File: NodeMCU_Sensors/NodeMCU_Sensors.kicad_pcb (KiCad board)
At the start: 2 copper layers, 71.1 x 40.6 mm, 12 parts, among them J1 Conn_02x15_Odd_Even, J2 Conn_02x15_Odd_Even, SW1 SW_Push

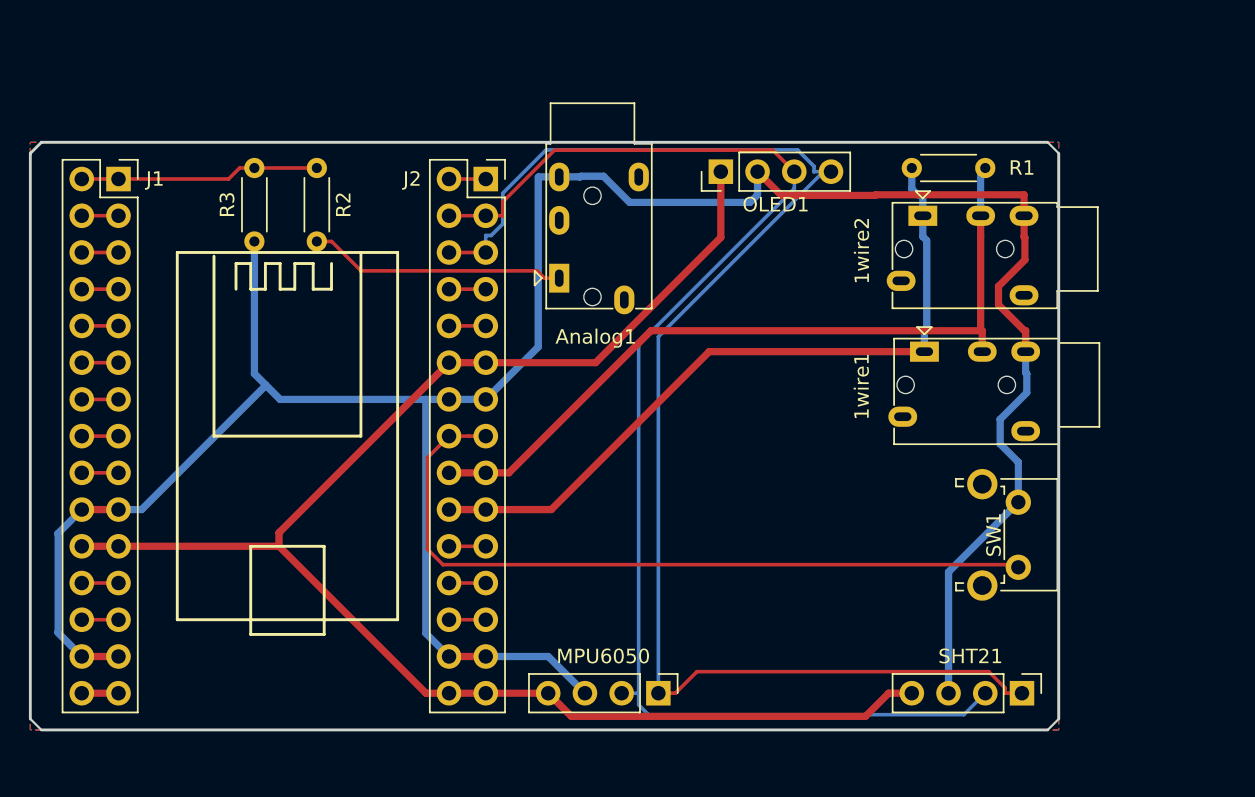
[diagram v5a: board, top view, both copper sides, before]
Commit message: Add 3V3 supply to analog pin and re-route
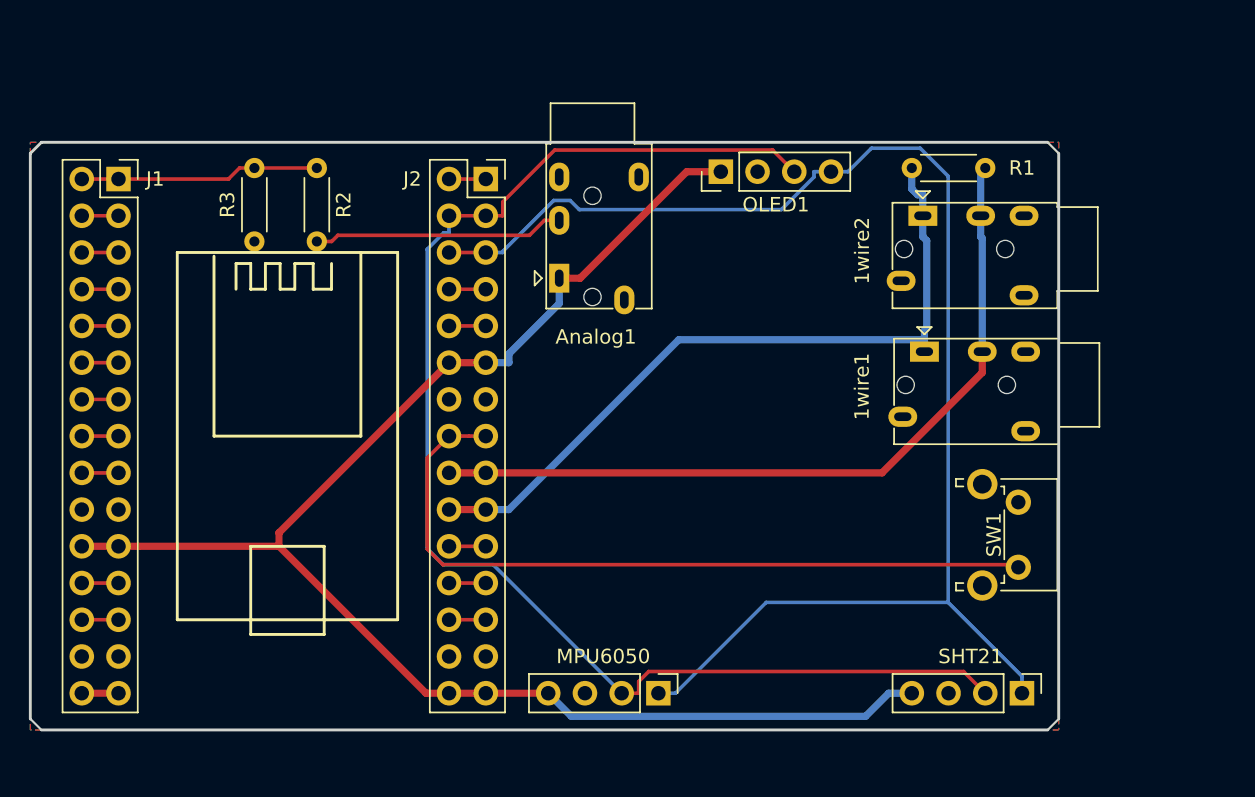
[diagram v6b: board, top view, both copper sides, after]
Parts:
- R2: value 39K -> 23.2K
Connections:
- Analog1 pad 1: Net-(Analog1-Pad1) -> 3V3
- R2 pad 2: Net-(Analog1-Pad1) -> Net-(Analog1-Pad2)
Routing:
- net GND: track 178.3 -> 0.00 mm
- net Net-(Analog1-Pad1): track 17.8 -> 0.00 mm
- net Net-(Analog1-Pad2): track 0.00 -> 17.4 mm
- net 3V3: track 107.4 -> 106.2 mm
- net D1: track 94.3 -> 95.3 mm
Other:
- board text added: "NodeMCU Sensor Node http://makesmart.io/ PCB: Whatnick INC v0.1 30/01/2018"
- board text removed: "NodeMCU Sensor Node Whatnick INC v0.1 28/01/2018"

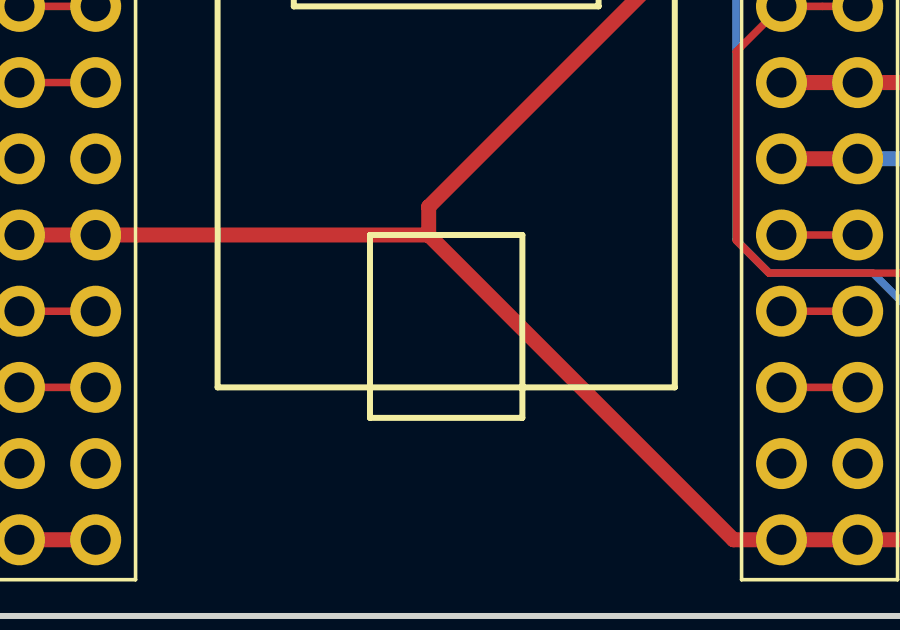
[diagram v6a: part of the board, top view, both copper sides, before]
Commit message: Adde makesmart logo
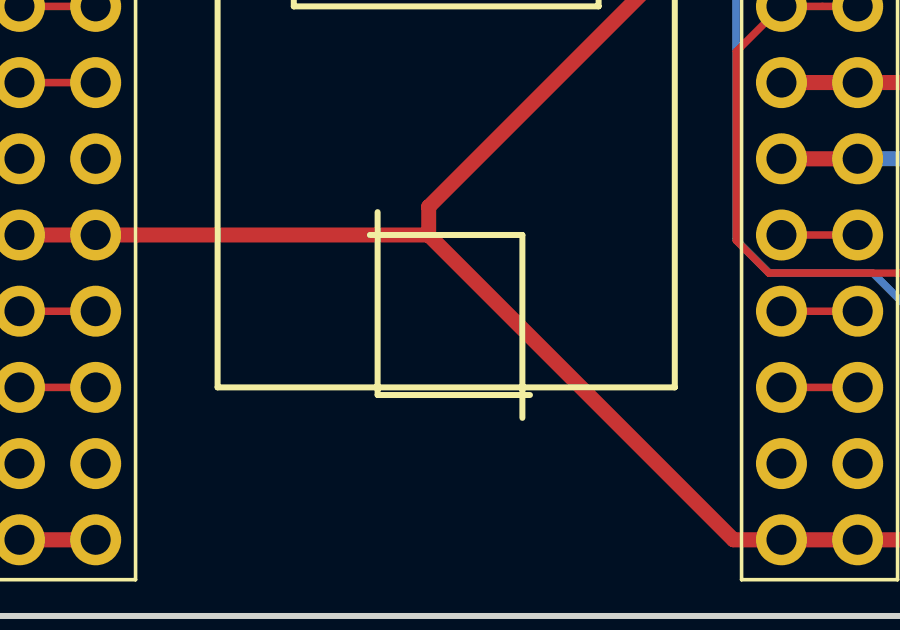
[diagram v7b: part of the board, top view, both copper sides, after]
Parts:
- added G1: LOGO, project_footprints:makeSmart_logo, B.Cu at (111.5, 81.0)
- added G2: Logo_Open_Hardware_Small, Symbols:OSHW-Logo2_7.3x6mm_SilkScreen, B.Cu at (111.3, 92.5)
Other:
- board text added: "TAPR"

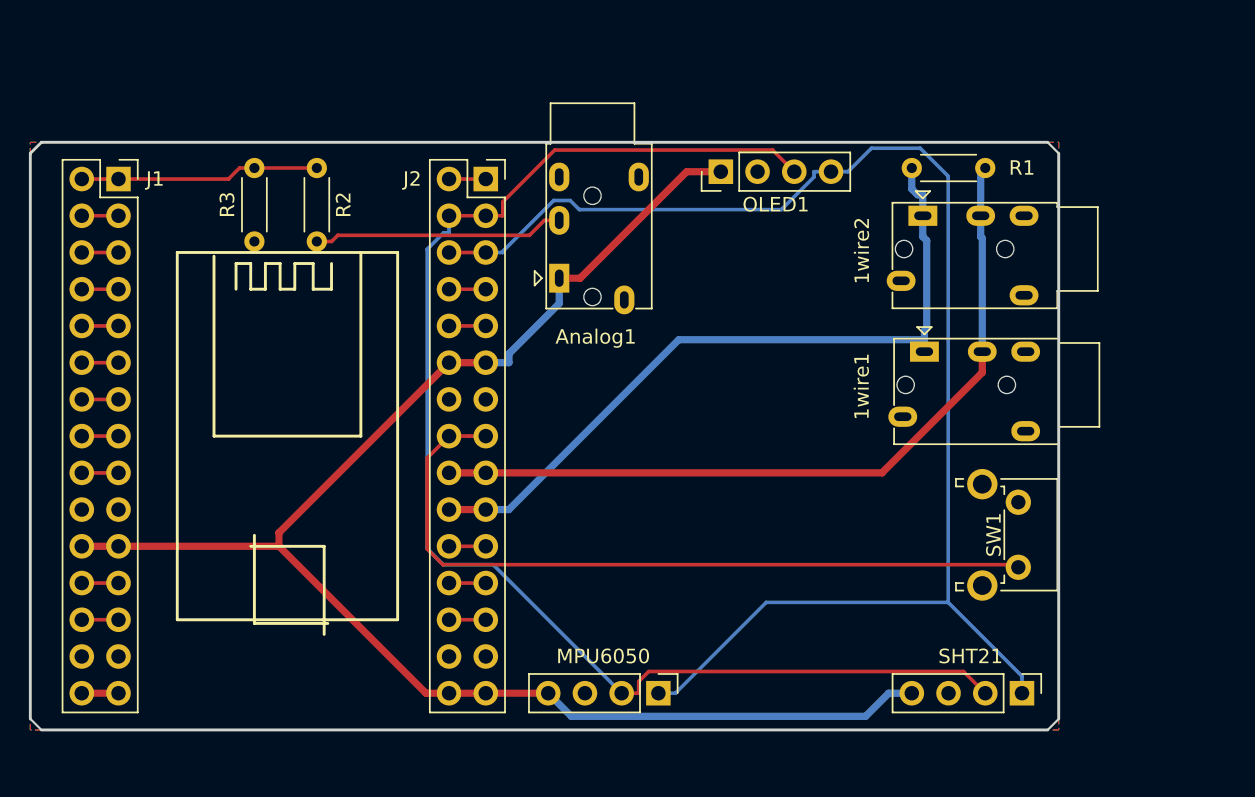
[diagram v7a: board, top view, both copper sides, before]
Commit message: Address #1 for V2 board
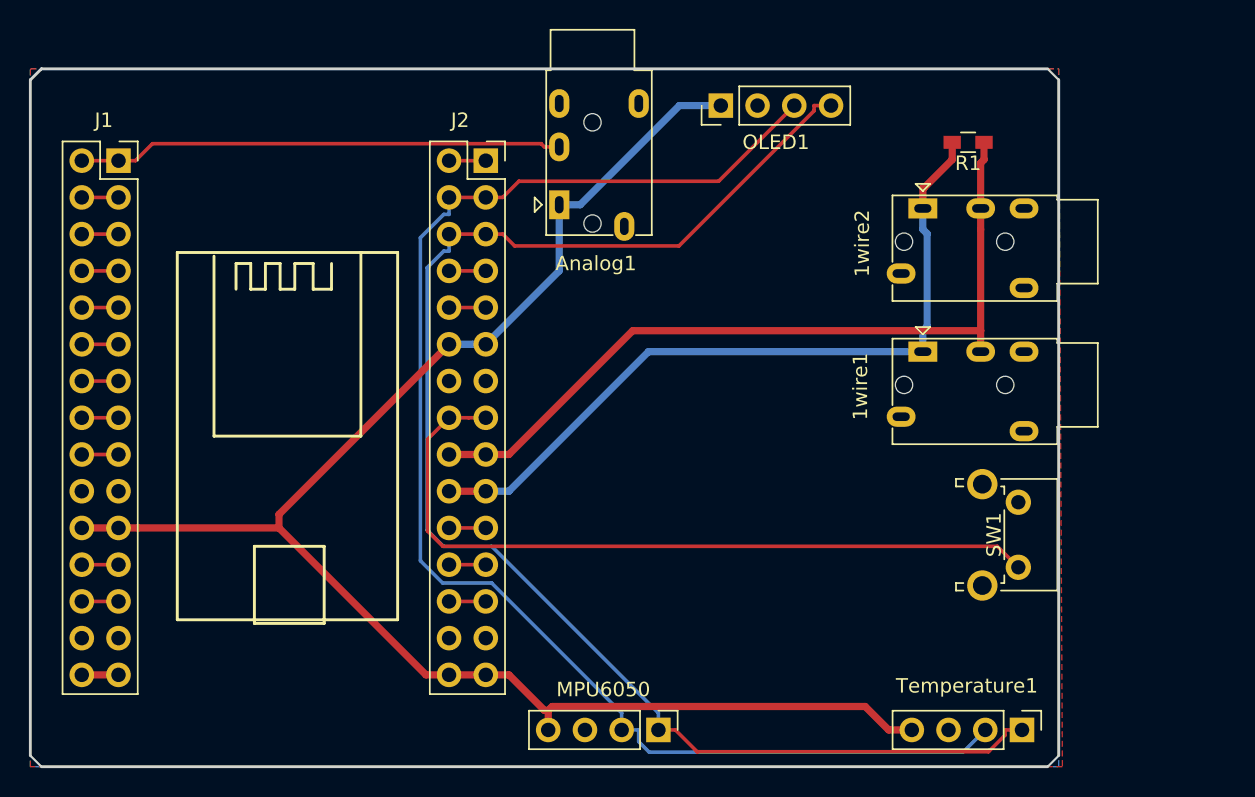
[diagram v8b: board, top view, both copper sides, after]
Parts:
- removed R2: 23.2K, Resistors_THT:R_Axial_DIN0204_L3.6mm_D1.6mm_P5.08mm_Horizontal
- removed R3: 10K, Resistors_THT:R_Axial_DIN0204_L3.6mm_D1.6mm_P5.08mm_Horizontal
- removed SHT21: Conn_01x04, Socket_Strips:Socket_Strip_Straight_1x04_Pitch2.54mm
- added Temperature1: Conn_01x04, Socket_Strips:Socket_Strip_Straight_1x04_Pitch2.54mm, F.Cu at (162.6, 104.1)
- R1: footprint Resistor_THT:R_Axial_DIN0204_L3.6mm_D1.6mm_P5.08mm_Horizontal -> Resistors_SMD:R_0603_HandSoldering
- moved Analog1 5.08 mm to (130.6, 67.8)
- moved OLED1 4.57 mm to (141.7, 61.0)
- moved MPU6050 2.54 mm to (137.4, 104.1)
- moved R1 2.14 mm to (158.8, 63.5)
- moved J1 1.27 mm to (100.1, 64.8)
- moved J2 1.27 mm to (125.5, 64.8)
- moved 1wire2 0.51 mm to (155.7, 68.1)
- moved 1wire1 0.11 mm to (155.7, 78.0)
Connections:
- Analog1 pad 2: Net-(Analog1-Pad2) -> A0
- Analog1 pad 3: GND -> Net-(Analog1-Pad3)
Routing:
- net Net-(Analog1-Pad2): track 17.4 -> 0.00 mm
- net A0: track 16.6 -> 33.6 mm
- net 3V3: track 106.2 -> 110.7 mm
- net D1: track 95.3 -> 99.0 mm
- net D2: track 99.6 -> 101.3 mm
- net D7: track 51.1 -> 52.4 mm
- net D6: track 54.1 -> 54.9 mm
- net D5: track 52.4 -> 52.9 mm
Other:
- board size 71.1 x 40.6 mm -> 71.1 x 48.3 mm
- board text added: "NodeMCU Sensor Node http://makesmart.io PCB: Whatnick INC v0.2 14/02/2018"
- board text removed: "NodeMCU Sensor Node http://makesmart.io/ PCB: Whatnick INC v0.1 30/01/2018"
